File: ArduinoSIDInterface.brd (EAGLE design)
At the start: 89.8 x 62.2 mm, 25 parts, among them IC1 74HC595N, IC2 74HC595N, T1 BC547

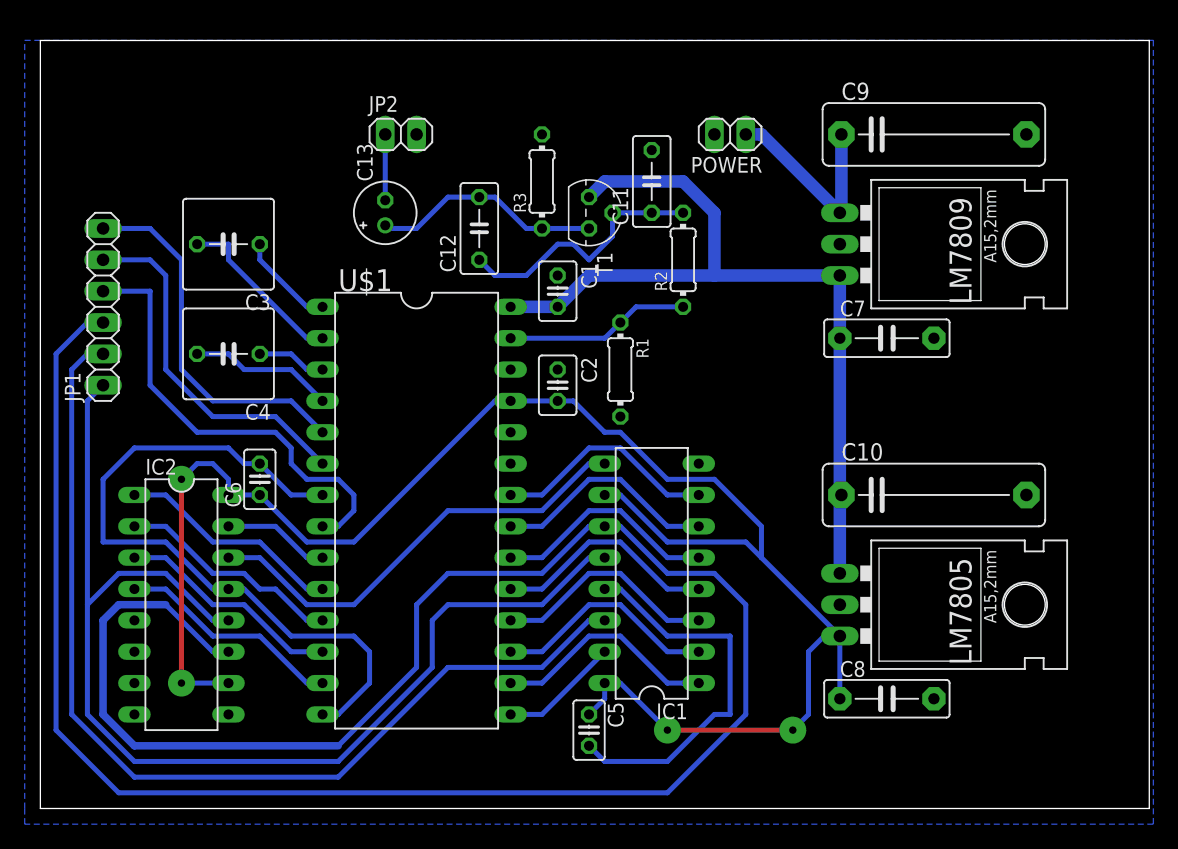
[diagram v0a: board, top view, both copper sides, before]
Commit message: Revised the schematic and board layout. Shift register->SID connections now inverted so Q7->D0 and Q0->D7. Requires a change to the SPI initialisation to be compatible but the board layout is a lot neater. Now only a single layer, no extra wires required. Make the power lines a lot thicker - I believe this is the thing to do. Added additional 5v power out header to power external Arduino.
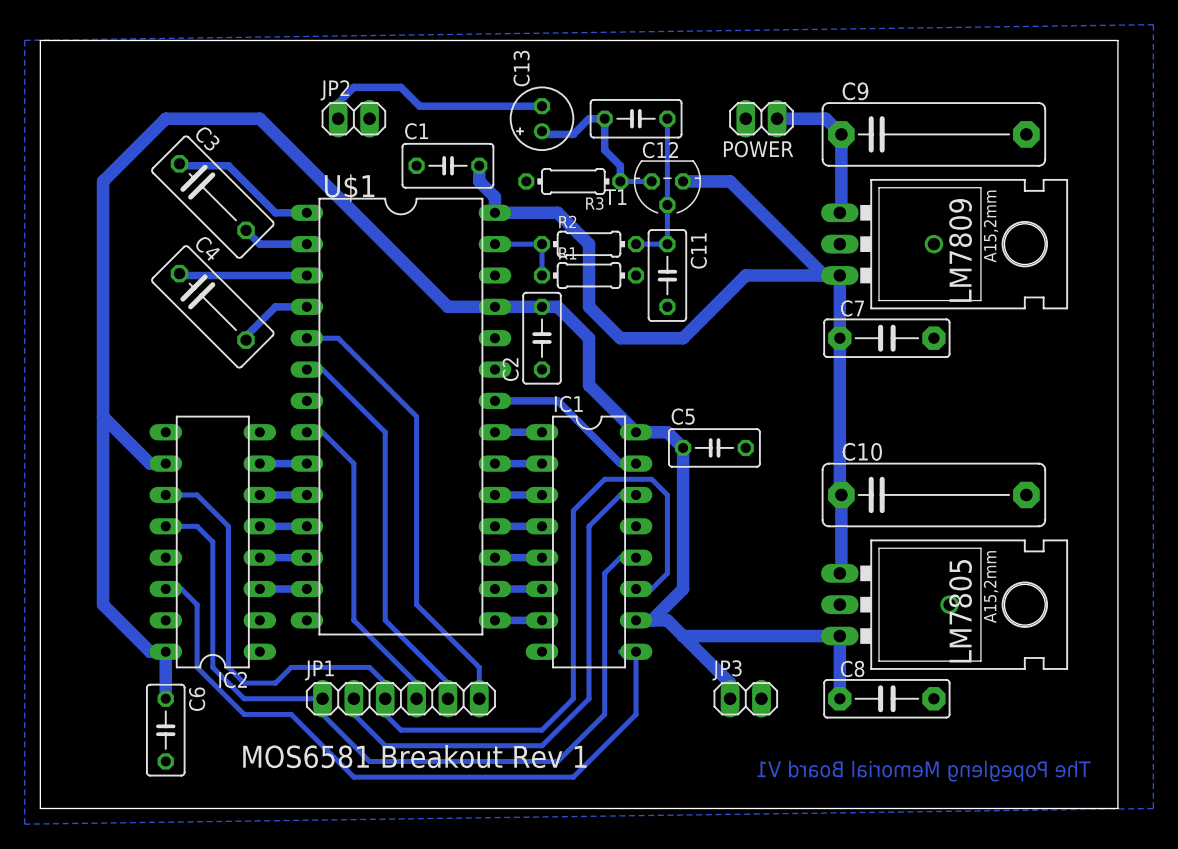
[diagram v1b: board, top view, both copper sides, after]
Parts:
- added JP3: (no value), pinhead:1X02
- C1: device rcl:C025-030X050 -> rcl:C050-035X075
- C2: device rcl:C025-030X050 -> rcl:C050-030X075
- C3, C4: device rcl:C050-075X075 -> rcl:C075-042X103
- C5, C6: device rcl:C025-025X050 -> rcl:C050-030X075
- moved JP1 39.9 mm to (29.2, 8.89), turned to 0 degrees
- moved C5 25.0 mm to (54.6, 29.2), turned to 0 degrees
- moved C6 21.7 mm to (10.2, 6.35), turned to 270 degrees
- moved C12 15.5 mm to (48.3, 55.9), turned to 180 degrees
- moved C13 14.8 mm to (40.6, 55.9)
- moved C1 13.5 mm to (33.0, 52.1), turned to 0 degrees
- moved R1 8.03 mm to (44.5, 43.2), turned to 0 degrees
- moved U$1 7.73 mm to (29.2, 31.8)
- moved C11 7.73 mm to (50.8, 43.2), turned to 270 degrees
- moved R2 7.73 mm to (44.5, 45.7), turned to 0 degrees
- moved T1 6.84 mm to (50.8, 50.8), turned to 180 degrees
- moved IC2 5.68 mm to (14.0, 21.6), turned to 90 degrees
- moved IC1 5.68 mm to (44.5, 21.6), turned to 270 degrees
- moved JP2 4.02 mm to (25.4, 55.9)
- moved C3 4.02 mm to (14.0, 49.5), turned to 315 degrees
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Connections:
- removed net N$10: IC1.1, U$1.16
- removed net N$13: IC1.4, U$1.19
- removed net N$14: IC1.2, U$1.17
- removed net N$15: IC1.3, U$1.18
- removed net N$18: IC1.6, U$1.21
- removed net N$19: IC1.7, U$1.22
- removed net N$8: IC1.5, U$1.20
- removed net N$9: IC1.15, U$1.15
- new net D0: IC1.7, U$1.15
- new net D1: IC1.6, U$1.16
- new net D2: IC1.5, U$1.17
- new net D3: IC1.4, U$1.18
- new net D4: IC1.3, U$1.19
- new net D5: IC1.2, U$1.20
- new net D6: IC1.1, U$1.21
- new net D7: IC1.15, U$1.22
- net GND: now also JP3.2
- net N$3: now also IC2.7; no longer IC2.15
- net N$4: now also IC2.6; no longer IC2.1
- net N$5: now also IC2.5; no longer IC2.2
- net N$6: now also IC2.4; no longer IC2.3
- net N$7: now also IC2.3; no longer IC2.4
- net VCC: now also JP3.1
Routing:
- net SCK: track 190.8 -> 85.1 mm
- net GND: track 89.8 -> 0.00 mm
- net SER: track 81.6 -> 41.8 mm
- net RCK: track 92.5 -> 66.2 mm
- net N$10: track 19.7 -> 0.00 mm
- net N$1: track 36.8 -> 55.8 mm
- net N$19: track 18.4 -> 0.00 mm
- net N$18: track 18.4 -> 0.00 mm
- net N$14: track 18.4 -> 0.00 mm
- net N$15: track 18.4 -> 0.00 mm
- net N$8: track 18.4 -> 0.00 mm, vias 0 -> 1
- net N$13: track 18.4 -> 0.00 mm
- net VCC: track 141.4 -> 158.9 mm, vias 4 -> 0
- net N$7: track 18.4 -> 3.81 mm
- net N$6: track 18.4 -> 3.81 mm
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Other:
- board size 89.8 x 62.2 mm -> 87.3 x 62.2 mm
- board text added: "MOS6581 Breakout Rev 1"
- board text added: "The Popegleng Memorial Board V1"

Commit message: Updated some packages on the schematic and slightly rearranged the board.
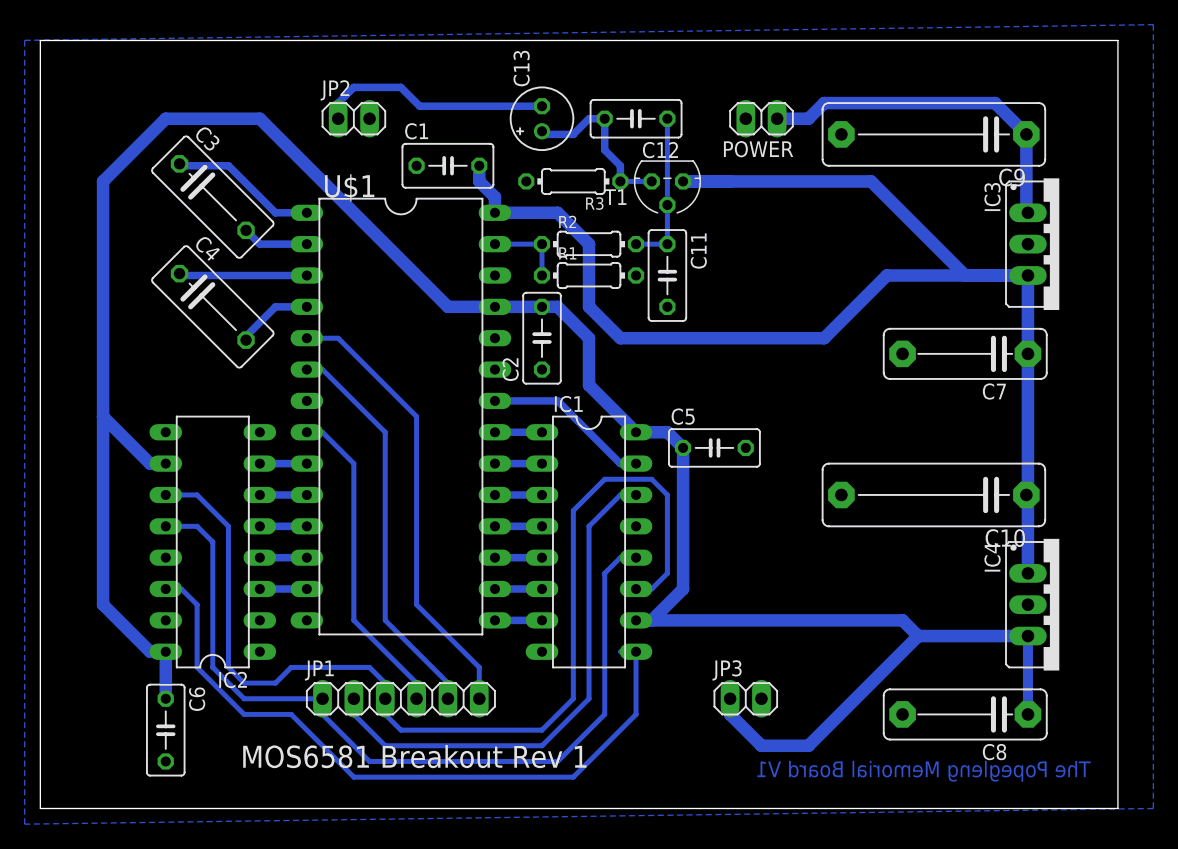
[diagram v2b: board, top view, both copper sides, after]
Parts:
- removed LM7805, LM7809: (no value), v-reg:78XXL
- added IC3: LM7809, v-reg:78XXS
- added IC4: LM7805, v-reg:78XXS
- C7, C8: device capacitor-wima:C7.5B3 -> capacitor-wima:C10B4
- moved C7 6.48 mm to (74.9, 36.8), turned to 180 degrees
- moved C8 6.48 mm to (74.9, 7.62), turned to 180 degrees
- turned C10 to 180 degrees
- turned C9 to 180 degrees
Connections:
- net GND: now also IC3.GND, IC4.GND; no longer LM7805.GND, LM7809.GND
- net V+: now also IC3.IN; no longer LM7809.IN
- net VCC: now also IC4.OUT; no longer LM7805.OUT
- net VDD: now also IC3.OUT, IC4.IN; no longer LM7805.IN, LM7809.OUT
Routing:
- net VDD: track 81.7 -> 115.9 mm
- net VCC: track 158.9 -> 188.7 mm
- net V+: track 12.1 -> 28.2 mm
